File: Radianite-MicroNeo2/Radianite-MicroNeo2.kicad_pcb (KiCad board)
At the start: 4 copper layers, 50 x 33 mm, 87 parts, among them J1 Micro_SD_Card_Det1, J2 USB_C_Receptacle_USB2.0_16P, J3 USB_C_Receptacle_USB2.0_16P, J4 AudioJack4, J6 Conn_02x16_Odd_Even, SW1 SW_Push, SW2 SW_SPDT, U1 F1C200s, U3 CH340E, U4 W25Q32JVZP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

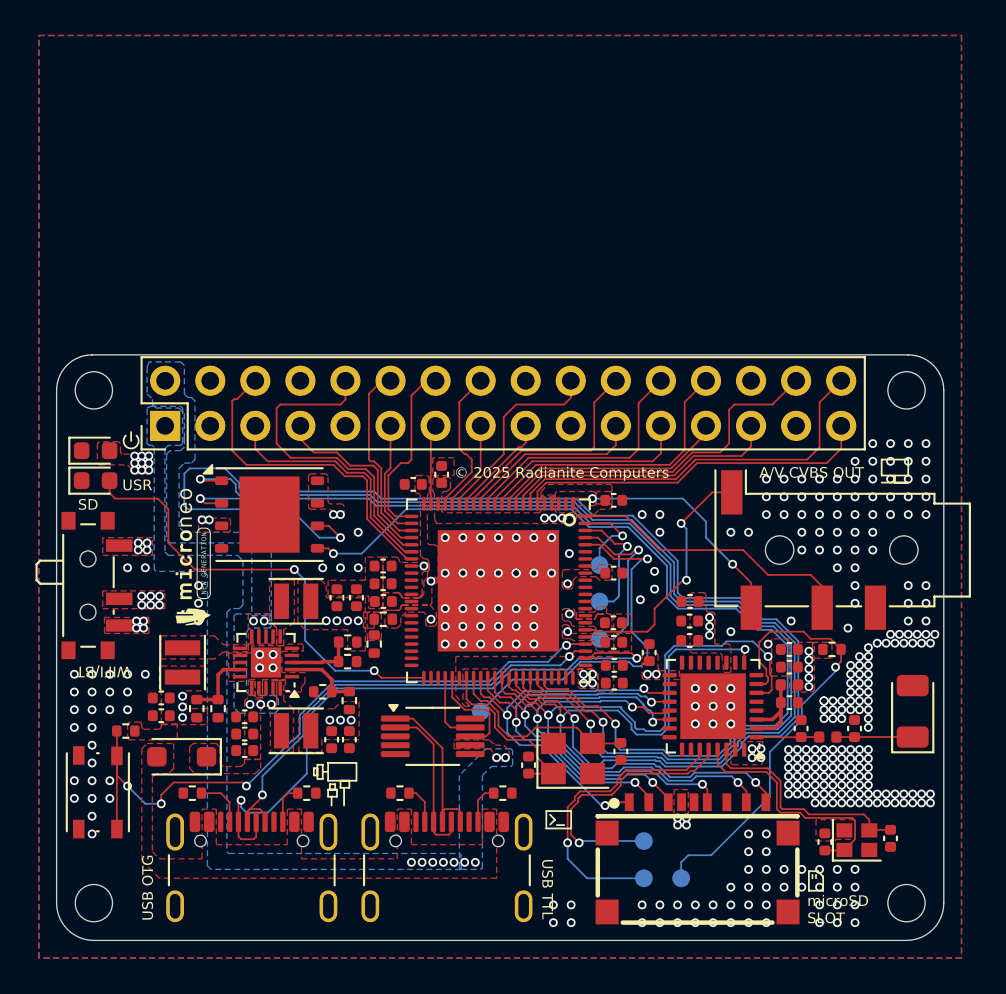
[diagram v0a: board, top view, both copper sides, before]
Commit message: fixing drc errors
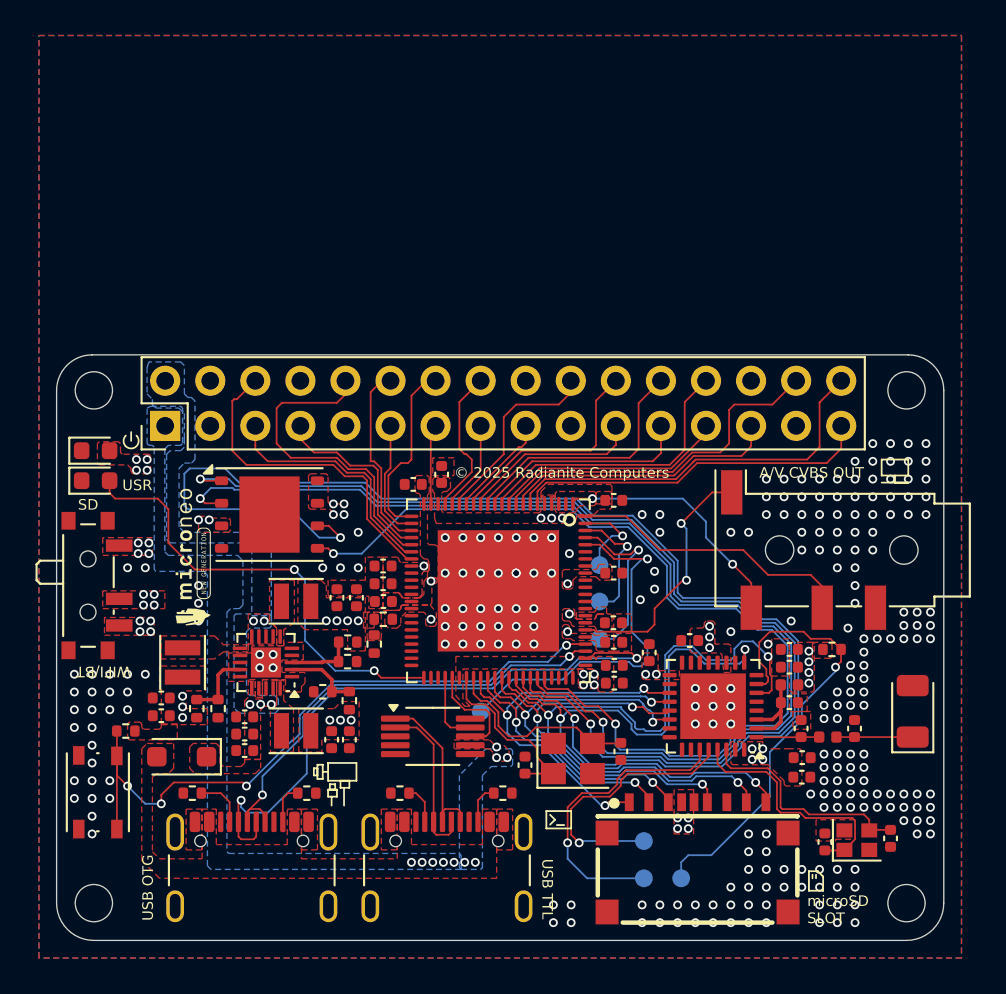
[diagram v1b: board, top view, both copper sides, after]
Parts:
- moved C28 11.7 mm to (122.0, 80.8), turned to 0 degrees
- moved C27 9.97 mm to (122.0, 79.7), turned to 0 degrees
- moved C10 0.20 mm to (106.4, 80.1)
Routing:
- net /SD_D1: track 35.4 -> 36.3 mm
- net /SD_D0: track 39.0 -> 39.9 mm
- net VBUS: vias 9 -> 10
- net GND: vias 324 -> 253
- net ESPVCC: vias 18 -> 17
- net +3V3: vias 30 -> 25

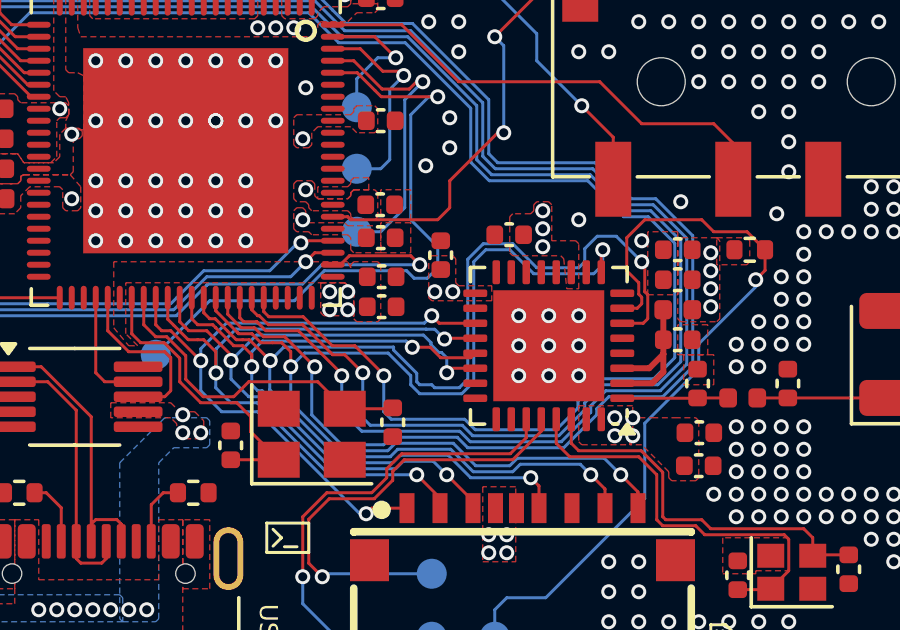
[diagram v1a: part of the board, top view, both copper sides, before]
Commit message: fix unreasoned wiggling traces that does not affect overall impedance and integrity
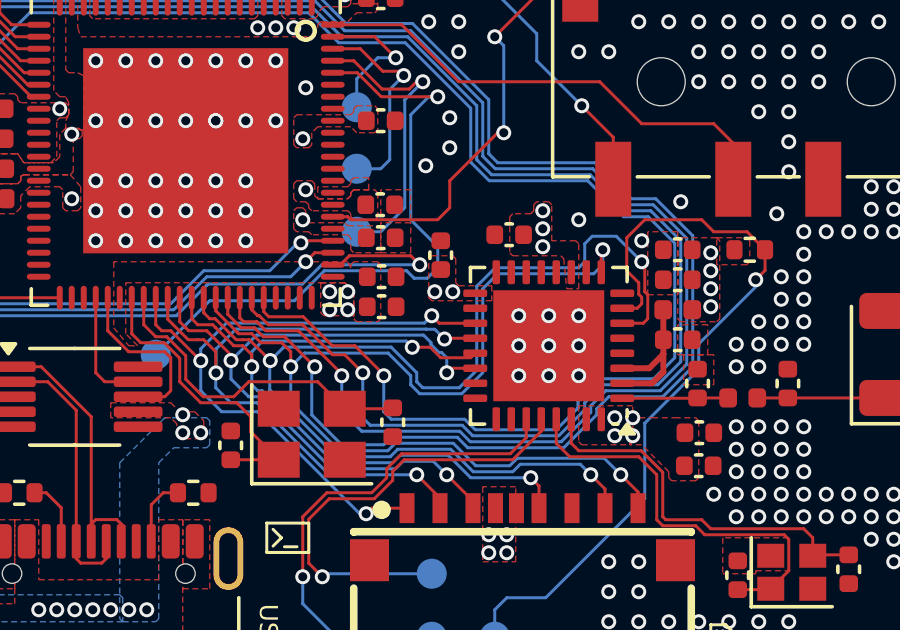
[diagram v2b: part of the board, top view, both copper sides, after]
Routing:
- net /SD_D1: track 36.3 -> 35.0 mm
- net /SD_D0: track 39.9 -> 38.6 mm
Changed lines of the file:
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@@
 	)
 	(segment
-		(start 114.817157 73.4)
-		(end 115.8 73.4)
-		(width 0.1)
-		(layer "B.Cu")
-		(net 25)
-	)
-	(segment
-		(start 113.2 78.2)
+		(start 112.8 78.2)
 		(end 114.017158 78.2)
 		(width 0.1)
@@
 	)
 	(segment
-		(start 114.3 73.917157)
-		(end 114.817157 73.4)
+		(start 112.6 78)
+		(end 112.8 78.2)
+		(width 0.1)
+		(layer "B.Cu")
+		(net 25)
+	)
+	(segment
+		(start 118.45 73.15)
+		(end 119.25 73.15)
 		(width 0.1)
 		(layer "B.Cu")
@@
 	)
 	(segment
+		(start 118 74.2)
+		(end 118.2 74)
+		(width 0.1)
+		(layer "B.Cu")
+		(net 25)
+	)
+	(segment
+		(start 118.2 73.4)
+		(end 118.45 73.15)
+		(width 0.1)
+		(layer "B.Cu")
+		(net 25)
+	)
+	(segment
+		(start 107.716647 77.294451)
+		(end 108.166647 76.844451)
+		(width 0.1)
+		(layer "B.Cu")
+		(net 25)
+	)
+	(segment
 		(start 113.732843 80.25)
 		(end 111.967158 80.25)
@@
 	)
 	(segment
-		(start 114.017158 78.2)
-		(end 114.3 77.917158)
-		(width 0.1)
-		(layer "B.Cu")
-		(net 25)
-	)
-	(segment
-		(start 112.7 78.1)
-		(end 113.1 78.1)
-		(width 0.1)
-		(layer "B.Cu")
-		(net 25)
-	)
-	(segment
-		(start 112.6 78)
-		(end 112.7 78.1)
+		(start 115.217157 74.2)
+		(end 118 74.2)
 		(width 0.1)
 		(layer "B.Cu")
@@
 	)
 	(segment
+		(start 111.744451 76.844451)
+		(end 112.6 77.7)
+		(width 0.1)
+		(layer "B.Cu")
+		(net 25)
+	)
+	(segment
+		(start 114.6 77.617158)
+		(end 114.6 74.817157)
+		(width 0.1)
+		(layer "B.Cu")
+		(net 25)
+	)
+	(segment
 		(start 108.166647 76.844451)
-		(end 111.827294 76.844451)
-		(width 0.1)
-		(layer "B.Cu")
-		(net 25)
-	)
-	(segment
-		(start 113.1 78.1)
-		(end 113.2 78.2)
-		(width 0.1)
-		(layer "B.Cu")
-		(net 25)
-	)
-	(segment
-		(start 112.6 77.717157)
-		(end 112.6 78)
-		(width 0.1)
-		(layer "B.Cu")
-		(net 25)
-	)
-	(segment
-		(start 118 74.2)
-		(end 118.2 74)
-		(width 0.1)
-		(layer "B.Cu")
-		(net 25)
-	)
-	(segment
-		(start 115.8 73.4)
-		(end 116.6 74.2)
+		(end 111.744451 76.844451)
+		(width 0.1)
+		(layer "B.Cu")
+		(net 25)
+	)
+	(segment
+		(start 119.25 73.15)
+		(end 120.1 74)
 		(width 0.1)
 		(layer "B.Cu")
@@
 	)
 	(segment
+		(start 118.2 74)
+		(end 118.2 73.4)
+		(width 0.1)
+		(layer "B.Cu")
+		(net 25)
+	)
+	(segment
+		(start 114.017158 78.2)
+		(end 114.6 77.617158)
+		(width 0.1)
+		(layer "B.Cu")
+		(net 25)
+	)
+	(segment
 		(start 107.7 77.311098)
 		(end 107.716647 77.294451)
@@
 	)
 	(segment
-		(start 111.827294 76.944451)
-		(end 112.6 77.717157)
-		(width 0.1)
-		(layer "B.Cu")
-		(net 25)
-	)
-	(segment
-		(start 116.6 74.2)
-		(end 118 74.2)
-		(width 0.1)
-		(layer "B.Cu")
-		(net 25)
-	)
-	(segment
-		(start 118.2 74)
-		(end 118.2 73.563603)
+		(start 112.6 77.7)
+		(end 112.6 78)
 		(width 0.1)
 		(layer "B.Cu")
@@
 	)
 	(segment
-		(start 118.2 73.563603)
-		(end 118.613603 73.15)
-		(width 0.1)
-		(layer "B.Cu")
-		(net 25)
-	)
-	(segment
-		(start 114.3 77.917158)
-		(end 114.3 73.917157)
-		(width 0.1)
-		(layer "B.Cu")
-		(net 25)
-	)
-	(segment
-		(start 111.827294 76.844451)
-		(end 111.827294 76.944451)
-		(width 0.1)
-		(layer "B.Cu")
-		(net 25)
-	)
-	(segment
-		(start 107.716647 77.294451)
-		(end 108.166647 76.844451)
+		(start 114.6 74.817157)
+		(end 115.217157 74.2)
 		(width 0.1)
 		(layer "B.Cu")
@@
 		(start 111.967158 80.25)
 		(end 111.717158 80.5)
-		(width 0.1)
-		(layer "B.Cu")
-		(net 25)
-	)
-	(segment
-		(start 118.613603 73.15)
-		(end 119.25 73.15)
-		(width 0.1)
-		(layer "B.Cu")
-		(net 25)
-	)
-	(segment
-		(start 119.25 73.15)
-		(end 120.1 74)
 		(width 0.1)
 		(layer "B.Cu")
@@
 	)
 	(segment
-		(start 114.5 74)
-		(end 114.5 78)
+		(start 118.8 73.6)
+		(end 118.8 74.1)
+		(width 0.1)
+		(layer "B.Cu")
+		(net 27)
+	)
+	(segment
+		(start 115.3 74.4)
+		(end 114.8 74.9)
 		(width 0.1)
 		(layer "B.Cu")
@@
 	)
 	(segment
+		(start 115.7 80.8)
+		(end 114.565685 80.8)
+		(width 0.1)
+		(layer "B.Cu")
+		(net 27)
+	)
+	(segment
+		(start 108.4 78.685789)
+		(end 108.4 77.5)
+		(width 0.1)
+		(layer "B.Cu")
+		(net 27)
+	)
+	(segment
 		(start 112.4 78.1)
 		(end 112.4 77.8)
@@
 	)
 	(segment
+		(start 111.884315 80.05)
+		(end 111.634315 80.3)
+		(width 0.1)
+		(layer "B.Cu")
+		(net 27)
+	)
+	(segment
+		(start 115.95 80.55)
+		(end 115.7 80.8)
+		(width 0.1)
+		(layer "B.Cu")
+		(net 27)
+	)
+	(segment
+		(start 114.8 77.7)
+		(end 114.1 78.4)
+		(width 0.1)
+		(layer "B.Cu")
+		(net 27)
+	)
+	(segment
+		(start 118.8 74.1)
+		(end 118.5 74.4)
+		(width 0.1)
+		(layer "B.Cu")
+		(net 27)
+	)
+	(segment
+		(start 114.8 74.9)
+		(end 114.8 77.7)
+		(width 0.1)
+		(layer "B.Cu")
+		(net 27)
+	)
+	(segment
+		(start 111.644451 77.044451)
+		(end 108.855549 77.044451)
+		(width 0.1)
+		(layer "B.Cu")
+		(net 27)
+	)
+	(segment
+		(start 111.634315 80.3)
+		(end 110.014211 80.3)
+		(width 0.1)
+		(layer "B.Cu")
+		(net 27)
+	)
+	(segment
 		(start 112.4 77.8)
 		(end 111.644451 77.044451)
@@
 	)
 	(segment
-		(start 115.7 80.8)
-		(end 114.565685 80.8)
-		(width 0.1)
-		(layer "B.Cu")
-		(net 27)
-	)
-	(segment
-		(start 108.4 78.685789)
+		(start 113.815685 80.05)
+		(end 111.884315 80.05)
+		(width 0.1)
+		(layer "B.Cu")
+		(net 27)
+	)
+	(segment
+		(start 118.5 74.4)
+		(end 115.3 74.4)
+		(width 0.1)
+		(layer "B.Cu")
+		(net 27)
+	)
+	(segment
+		(start 114.1 78.4)
+		(end 112.7 78.4)
+		(width 0.1)
+		(layer "B.Cu")
+		(net 27)
+	)
+	(segment
+		(start 108.855549 77.044451)
 		(end 108.4 77.5)
 		(width 0.1)
@@
 	)
 	(segment
-		(start 111.884315 80.05)
-		(end 111.634315 80.3)
-		(width 0.1)
-		(layer "B.Cu")
-		(net 27)
-	)
-	(segment
-		(start 115.95 80.55)
-		(end 115.7 80.8)
-		(width 0.1)
-		(layer "B.Cu")
-		(net 27)
-	)
-	(segment
-		(start 116.5 74.4)
-		(end 115.7 73.6)
-		(width 0.1)
-		(layer "B.Cu")
-		(net 27)
-	)
-	(segment
-		(start 116.5 74.4)
-		(end 118.5 74.4)
-		(width 0.1)
-		(layer "B.Cu")
-		(net 27)
-	)
-	(segment
-		(start 111.644451 77.044451)
-		(end 108.855549 77.044451)
+		(start 118.85 80.55)
+		(end 115.95 80.55)
 		(width 0.1)
 		(layer "B.Cu")
@@
 	)
 	(segment
-		(start 118.5 74.4)
-		(end 118.8 74.1)
-		(width 0.1)
-		(layer "B.Cu")
-		(net 27)
-	)
-	(segment
-		(start 111.634315 80.3)
-		(end 110.014211 80.3)
-		(width 0.1)
-		(layer "B.Cu")
-		(net 27)
-	)
-	(segment
-		(start 113.815685 80.05)
-		(end 111.884315 80.05)
-		(width 0.1)
-		(layer "B.Cu")
-		(net 27)
-	)
-	(segment
-		(start 114.1 78.4)
-		(end 112.7 78.4)
-		(width 0.1)
-		(layer "B.Cu")
-		(net 27)
-	)
-	(segment
-		(start 115.7 73.6)
-		(end 114.9 73.6)
-		(width 0.1)
-		(layer "B.Cu")
-		(net 27)
-	)
-	(segment
-		(start 114.9 73.6)
-		(end 114.5 74)
-		(width 0.1)
-		(layer "B.Cu")
-		(net 27)
-	)
-	(segment
-		(start 118.85 80.55)
-		(end 115.95 80.55)
-		(width 0.1)
-		(layer "B.Cu")
-		(net 27)
-	)
-	(segment
-		(start 118.8 74.1)
-		(end 118.8 73.6)
-		(width 0.1)
-		(layer "B.Cu")
-		(net 27)
-	)
-	(segment
-		(start 108.855549 77.044451)
-		(end 108.4 77.5)
-		(width 0.1)
-		(layer "B.Cu")
-		(net 27)
-	)
-	(segment
 		(start 119.4 81.1)
 		(end 118.85 80.55)
 		(width 0.1)
 		(layer "B.Cu")
-		(net 27)
-	)
-	(segment
-		(start 114.5 78)
-		(end 114.1 78.4)
-		(width 0.1)
-		(layer "B.Cu")
